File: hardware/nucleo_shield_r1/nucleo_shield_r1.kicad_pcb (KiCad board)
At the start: 2 copper layers, 70 x 80 mm, 16 parts, among them J101 UART, J102 UART SELECTOR, J103 SWD, J104 SWD Header, J105 Conn_01x10, J106 POWER, J107 Conn_01x06, J108 Conn_01x08, Q101 Q_Dual_NMOS_S1G1D2S2G2D1, Q102 Q_Dual_NMOS_S1G1D2S2G2D1

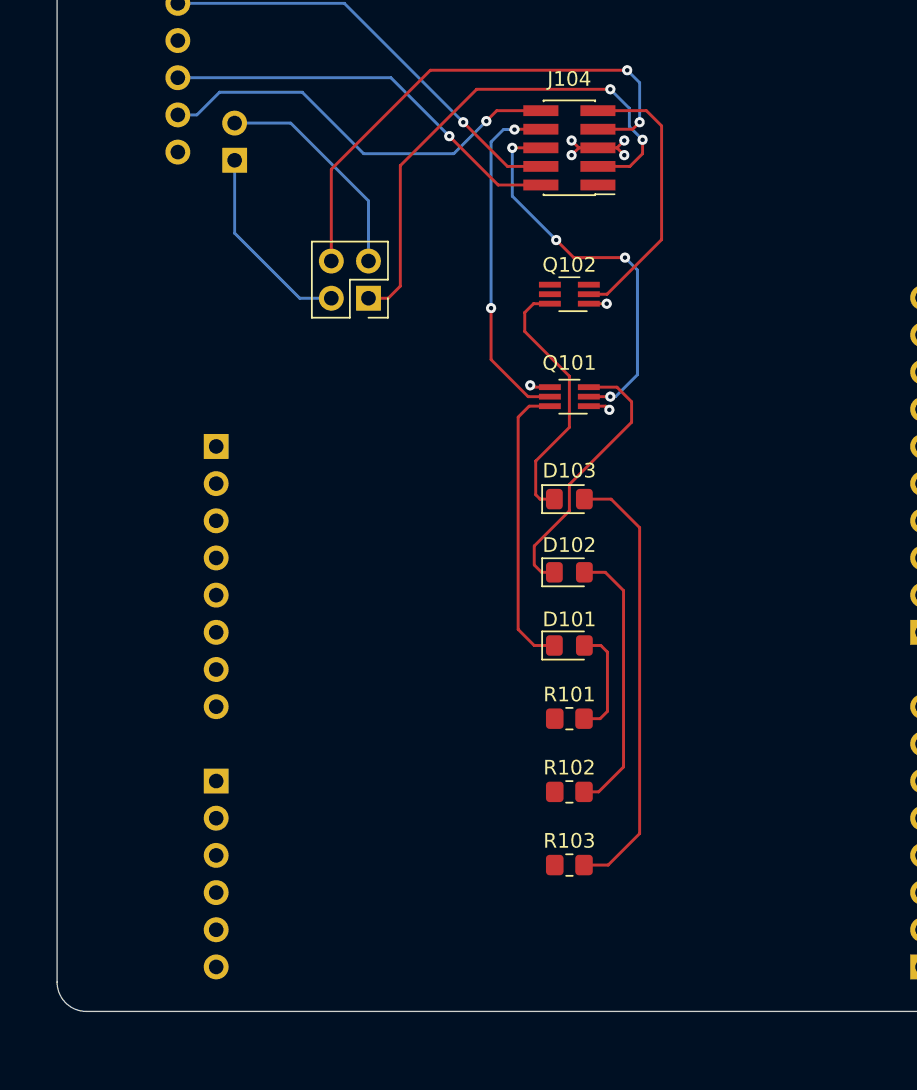
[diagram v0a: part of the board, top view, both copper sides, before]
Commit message: Next revision of the boards are finished and ready for fabrication, and a BOM has been added.
The BOM is still missing components for the nucleo shield.
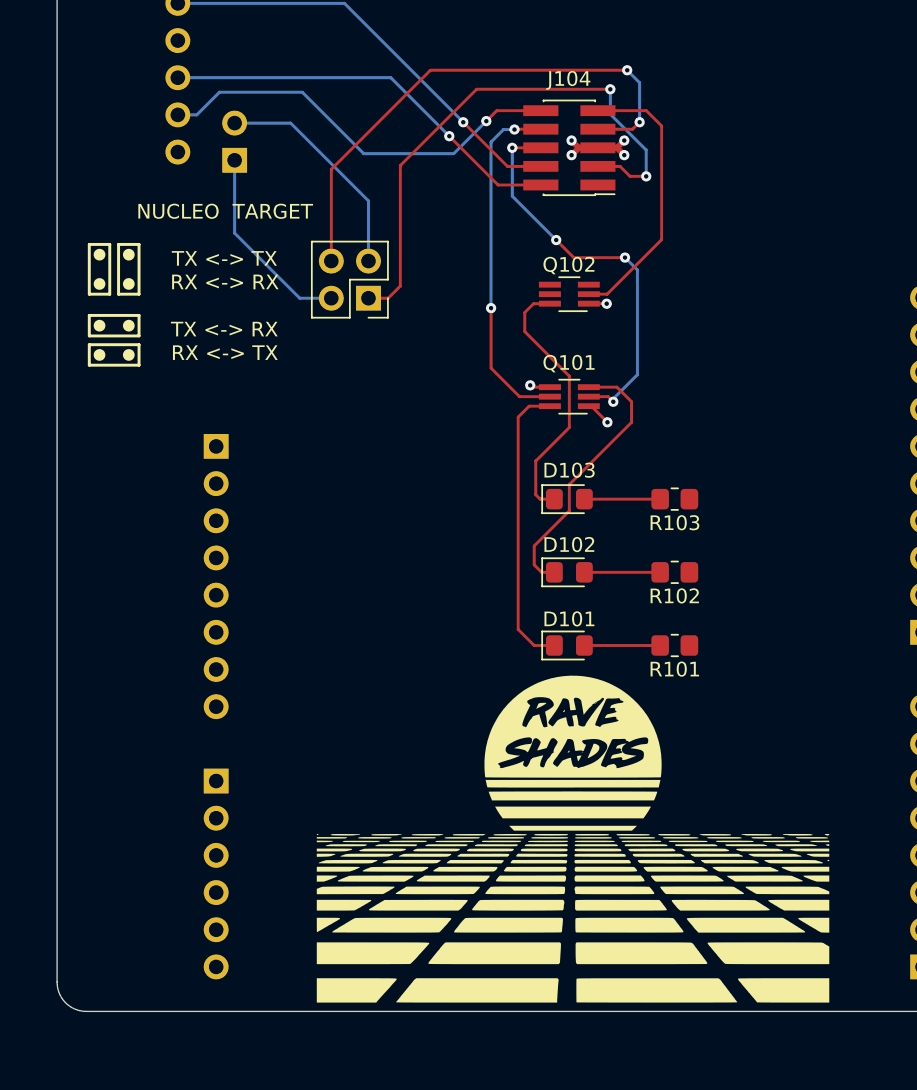
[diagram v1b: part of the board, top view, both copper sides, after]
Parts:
- added G***: LOGO, rave_shades:logo_size_3, F.Cu at (147.2, 123.0)
- moved R103 26.0 mm to (154.2, 101.0), turned to 180 degrees
- moved R102 16.6 mm to (154.2, 106.0), turned to 180 degrees
- moved R101 8.77 mm to (154.2, 111.0), turned to 180 degrees
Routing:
- net Net-(D103-Pad2): track 30.2 -> 5.17 mm
- net Net-(D102-Pad2): track 18.6 -> 5.17 mm
- net Net-(D101-Pad2): track 7.62 -> 5.17 mm
- net /DBG_UART_RX: track 36.0 -> 37.8 mm
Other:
- rule pad_to_mask_clearance: 0.05 -> 0
- board text added: "NUCLEO SHIELD R1"
- board text added: "NUCLEO TARGET TX <-> TX RX <-> RX TX <-> RX RX <-> TX"
